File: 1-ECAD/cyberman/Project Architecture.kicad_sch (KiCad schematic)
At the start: 0 parts

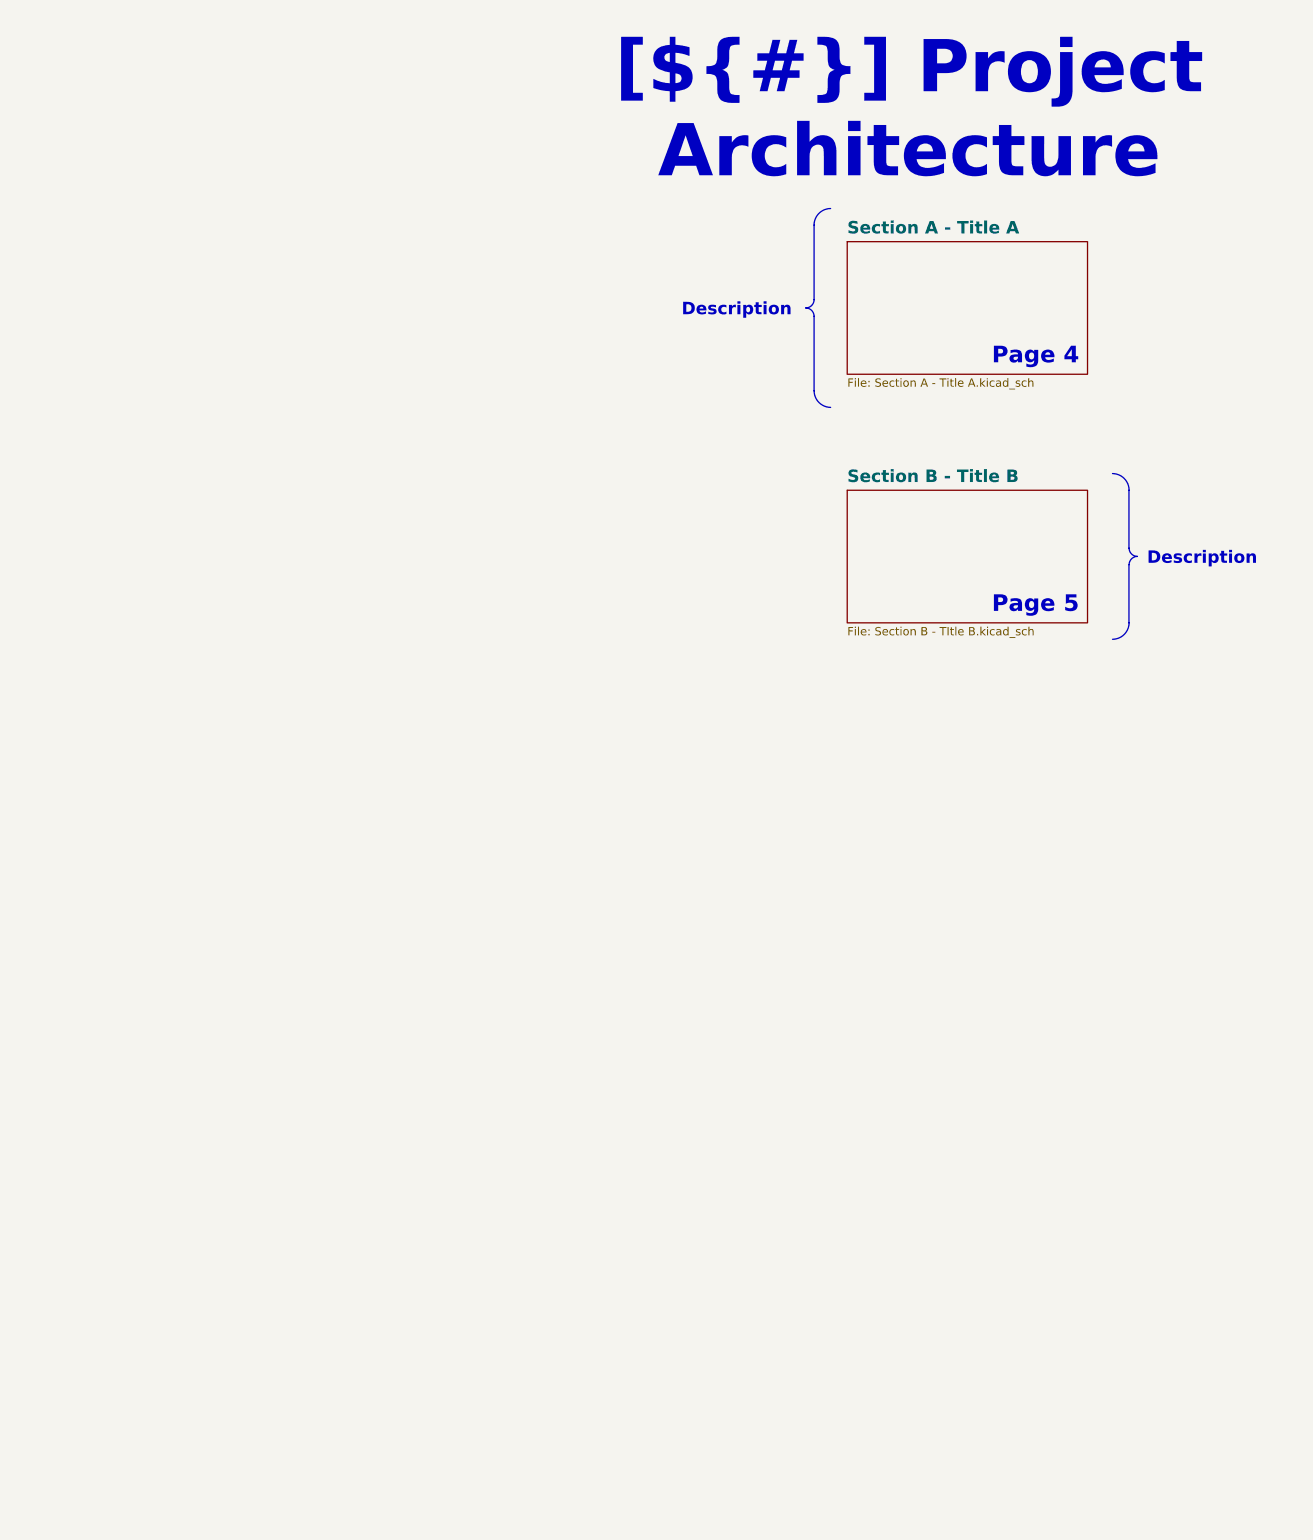
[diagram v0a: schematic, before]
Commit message: esp32 supply
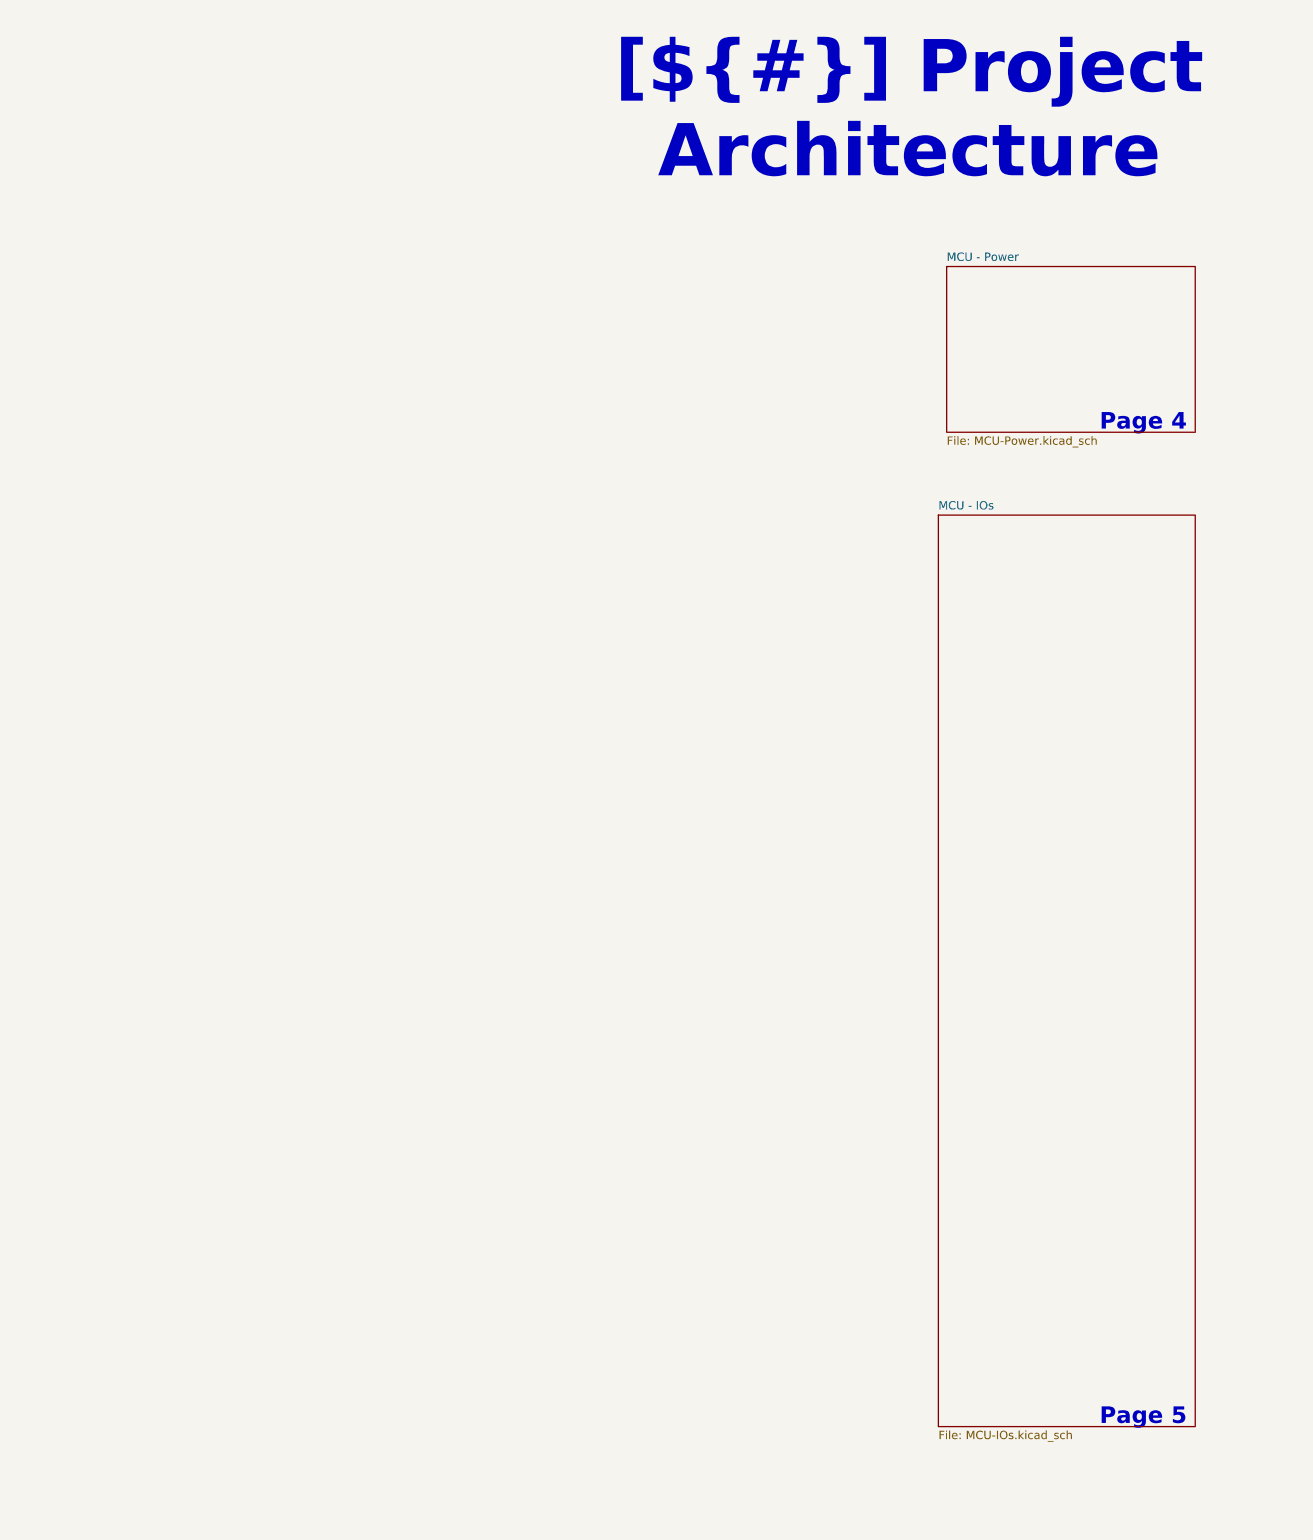
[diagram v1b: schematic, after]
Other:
- removed sheet Section A - Title A
- removed sheet Section B - Title B
- added sheet MCU - IOs (MCU-IOs.kicad_sch)
- added sheet MCU - Power (MCU-Power.kicad_sch)
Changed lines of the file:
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@@
 		(company "${COMPANY}")
-	)
-	(polyline
-		(pts
-			(xy 195.58 58.42) (xy 195.58 69.85)
-		)
-		(stroke
-			(width 0)
-			(type default)
-		)
-	)
-	(polyline
-		(pts
-			(xy 195.58 55.88) (xy 195.58 44.45)
-		)
-		(stroke
-			(width 0)
-			(type default)
-		)
-	)
-	(polyline
-		(pts
-			(xy 243.84 85.09) (xy 243.84 93.98)
-		)
-		(stroke
-			(width 0)
-			(type default)
-		)
-	)
-	(polyline
-		(pts
-			(xy 243.84 96.52) (xy 243.84 105.41)
-		)
-		(stroke
-			(width 0)
-			(type default)
-		)
-	)
-	(arc
-		(start 243.86 96.5)
-		(mid 244.2349 95.6049)
-		(end 245.13 95.23)
-		(stroke
-			(width 0)
-			(type default)
-		)
-		(fill
-			(type none)
-		)
-	)
-	(arc
-		(start 195.58 55.88)
-		(mid 195.2051 56.7751)
-		(end 194.31 57.15)
-		(stroke
-			(width 0)
-			(type default)
-		)
-		(fill
-			(type none)
-		)
-	)
-	(arc
-		(start 241.32 82.53)
-		(mid 243.1102 83.2798)
-		(end 243.86 85.07)
-		(stroke
-			(width 0)
-			(type default)
-		)
-		(fill
-			(type none)
-		)
-	)
-	(arc
-		(start 194.31 57.15)
-		(mid 195.2051 57.5249)
-		(end 195.58 58.42)
-		(stroke
-			(width 0)
-			(type default)
-		)
-		(fill
-			(type none)
-		)
-	)
-	(arc
-		(start 243.86 105.39)
-		(mid 243.1161 107.1861)
-		(end 241.32 107.93)
-		(stroke
-			(width 0)
-			(type default)
-		)
-		(fill
-			(type none)
-		)
-	)
-	(arc
-		(start 245.13 95.23)
-		(mid 244.2349 94.8551)
-		(end 243.86 93.96)
-		(stroke
-			(width 0)
-			(type default)
-		)
-		(fill
-			(type none)
-		)
-	)
-	(arc
-		(start 195.58 44.45)
-		(mid 196.3239 42.6539)
-		(end 198.12 41.91)
-		(stroke
-			(width 0)
-			(type default)
-		)
-		(fill
-			(type none)
-		)
-	)
-	(arc
-		(start 198.12 72.39)
-		(mid 196.3298 71.6402)
-		(end 195.58 69.85)
-		(stroke
-			(width 0)
-			(type default)
-		)
-		(fill
-			(type none)
-		)
-	)
-	(text_box "Description"
-		(exclude_from_sim no)
-		(at 176.53 54.61 0)
-		(size 17.145 5.08)
-		(stroke
-			(width -0.0001)
-			(type default)
-		)
-		(fill
-			(type none)
-		)
-		(effects
-			(font
-				(size 1.905 1.905)
-				(thickness 0.381)
-				(bold yes)
-				(color 0 0 0 1)
-			)
-			(justify right top)
-		)
 	)
 	(text_box "[${#}] ${TITLE}"
@@
 		)
 	)
-	(text_box "Description"
-		(exclude_from_sim no)
-		(at 245.11 92.71 0)
-		(size 26.015 5.1)
-		(stroke
-			(width -0.0001)
-			(type default)
-		)
-		(fill
-			(type none)
-		)
-		(effects
-			(font
-				(size 1.905 1.905)
-				(thickness 0.381)
-				(bold yes)
-				(color 0 0 0 1)
-			)
-			(justify left top)
-		)
-	)
 	(text "Page 4"
 		(exclude_from_sim no)
-		(at 236.22 66.04 0)
+		(at 252.73 76.2 0)
 		(effects
 			(font
@@
 	(text "Page 5"
 		(exclude_from_sim no)
-		(at 236.22 104.14 0)
+		(at 252.73 228.6 0)
 		(effects
 			(font
@@
 	)
 	(sheet
-		(at 200.66 46.99)
-		(size 36.83 20.32)
+		(at 215.9 50.8)
+		(size 38.1 25.4)
 		(fields_autoplaced yes)
 		(stroke
@@
 		)
 		(fill
-			(color 128 255 128 0.5000)
+			(color 0 194 0 0.5000)
 		)
-		(property "Sheetname" "Section A - Title A"
-			(at 200.66 45.9609 0)
+		(property "Sheetname" "MCU - Power"
+			(at 215.9 50.0884 0)
 			(effects
 				(font
-					(size 1.905 1.905)
-					(bold yes)
+					(size 1.27 1.27)
 				)
 				(justify left bottom)
 			)
 		)
-		(property "Sheetfile" "Section A - Title A.kicad_sch"
-			(at 200.66 67.8946 0)
+		(property "Sheetfile" "MCU-Power.kicad_sch"
+			(at 215.9 76.7846 0)
 			(effects
 				(font
-					(face "Arial")
 					(size 1.27 1.27)
 				)
@@
 	)
 	(sheet
-		(at 200.66 85.09)
-		(size 36.83 20.32)
+		(at 214.63 88.9)
+		(size 39.37 139.7)
 		(fields_autoplaced yes)
 		(stroke
@@
 		)
 		(fill
-			(color 255 200 0 0.5020)
+			(color 0 255 255 0.5000)
 		)
-		(property "Sheetname" "Section B - Title B"
-			(at 200.66 84.0609 0)
+		(property "Sheetname" "MCU - IOs"
+			(at 214.63 88.1884 0)
 			(effects
 				(font
-					(size 1.905 1.905)
-					(bold yes)
+					(size 1.27 1.27)
 				)
 				(justify left bottom)
 			)
 		)
-		(property "Sheetfile" "Section B - TItle B.kicad_sch"
-			(at 200.66 105.9946 0)
+		(property "Sheetfile" "MCU-IOs.kicad_sch"
+			(at 214.63 229.1846 0)
 			(effects
 				(font
-					(face "Arial")
 					(size 1.27 1.27)
 				)

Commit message: power
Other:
- added sheet Power (power.kicad_sch)
- sheet MCU - IOs: file MCU-IOs.kicad_sch -> mcu-IOs.kicad_sch
- sheet MCU - Power: file MCU-Power.kicad_sch -> mcu-power.kicad_sch
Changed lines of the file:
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@@
 	(text "Page 4"
 		(exclude_from_sim no)
-		(at 252.73 76.2 0)
+		(at 252.73 74.93 0)
 		(effects
 			(font
@@
 	(text "Page 5"
 		(exclude_from_sim no)
-		(at 252.73 228.6 0)
+		(at 252.73 227.33 0)
 		(effects
 			(font
@@
 			(justify right bottom)
 			(href "#5")
+		)
+	)
+	(sheet
+		(at 88.9 50.8)
+		(size 38.1 25.4)
+		(fields_autoplaced yes)
+		(stroke
+			(width 0.1524)
+			(type solid)
+		)
+		(fill
+			(color 255 0 0 0.5000)
+		)
+		(property "Sheetname" "Power"
+			(at 88.9 50.0884 0)
+			(effects
+				(font
+					(size 1.27 1.27)
+				)
+				(justify left bottom)
+			)
+		)
+		(property "Sheetfile" "power.kicad_sch"
+			(at 88.9 76.7846 0)
+			(effects
+				(font
+					(size 1.27 1.27)
+				)
+				(justify left top)
+			)
+		)
+		(instances
+			(project "cyberman"
+				(path "/0650c7a8-acba-429c-9f8e-eec0baf0bc1c/fede4c36-00cc-4d3d-b71c-5243ba232202"
+					(page "7")
+				)
+			)
 		)
 	)
@@
 			)
 		)
-		(property "Sheetfile" "MCU-Power.kicad_sch"
+		(property "Sheetfile" "mcu-power.kicad_sch"
 			(at 215.9 76.7846 0)
 			(effects
@@
 			)
 		)
-		(property "Sheetfile" "MCU-IOs.kicad_sch"
+		(property "Sheetfile" "mcu-IOs.kicad_sch"
 			(at 214.63 229.1846 0)
 			(effects

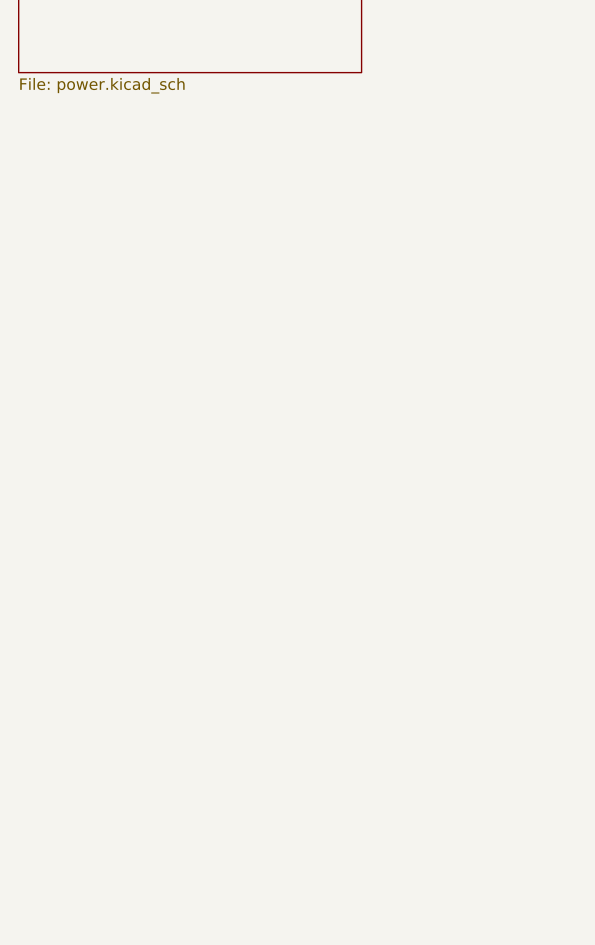
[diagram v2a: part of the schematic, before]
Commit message: microSD and LCD connector
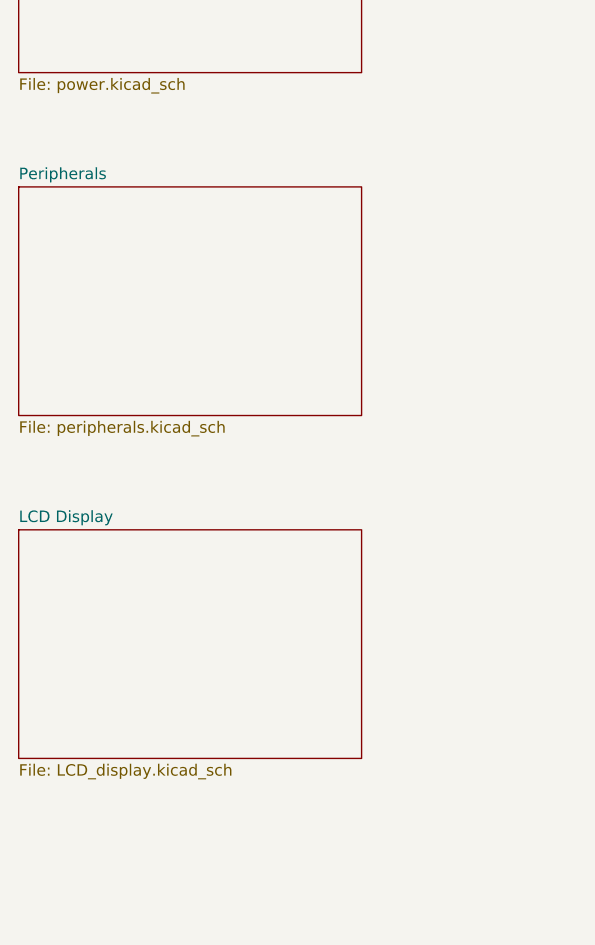
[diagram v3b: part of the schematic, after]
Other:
- added sheet LCD Display (LCD_display.kicad_sch)
- added sheet Peripherals (peripherals.kicad_sch)
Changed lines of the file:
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@@
+	)
+	(sheet
+		(at 88.9 127)
+		(size 38.1 25.4)
+		(fields_autoplaced yes)
+		(stroke
+			(width 0.1524)
+			(type solid)
+		)
+		(fill
+			(color 0 255 0 0.5000)
+		)
+		(property "Sheetname" "LCD Display"
+			(at 88.9 126.2884 0)
+			(effects
+				(font
+					(size 1.27 1.27)
+				)
+				(justify left bottom)
+			)
+		)
+		(property "Sheetfile" "LCD_display.kicad_sch"
+			(at 88.9 152.9846 0)
+			(effects
+				(font
+					(size 1.27 1.27)
+				)
+				(justify left top)
+			)
+		)
+		(instances
+			(project "cyberman"
+				(path "/0650c7a8-acba-429c-9f8e-eec0baf0bc1c/fede4c36-00cc-4d3d-b71c-5243ba232202"
+					(page "9")
+				)
+			)
+		)
+	)
+	(sheet
+		(at 88.9 88.9)
+		(size 38.1 25.4)
+		(fields_autoplaced yes)
+		(stroke
+			(width 0.1524)
+			(type solid)
+		)
+		(fill
+			(color 255 153 0 0.5000)
+		)
+		(property "Sheetname" "Peripherals"
+			(at 88.9 88.1884 0)
+			(effects
+				(font
+					(size 1.27 1.27)
+				)
+				(justify left bottom)
+			)
+		)
+		(property "Sheetfile" "peripherals.kicad_sch"
+			(at 88.9 114.8846 0)
+			(effects
+				(font
+					(size 1.27 1.27)
+				)
+				(justify left top)
+			)
+		)
+		(instances
+			(project "cyberman"
+				(path "/0650c7a8-acba-429c-9f8e-eec0baf0bc1c/fede4c36-00cc-4d3d-b71c-5243ba232202"
+					(page "8")
+				)
+			)
+		)
 	)
 	(sheet

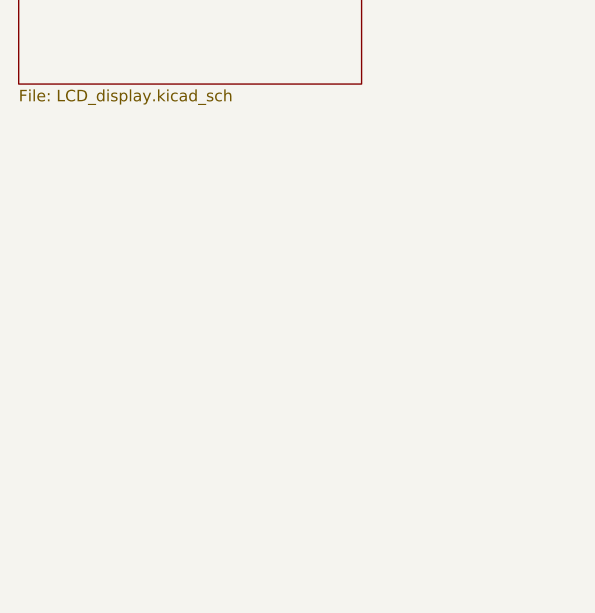
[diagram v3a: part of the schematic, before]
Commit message: add sensor page
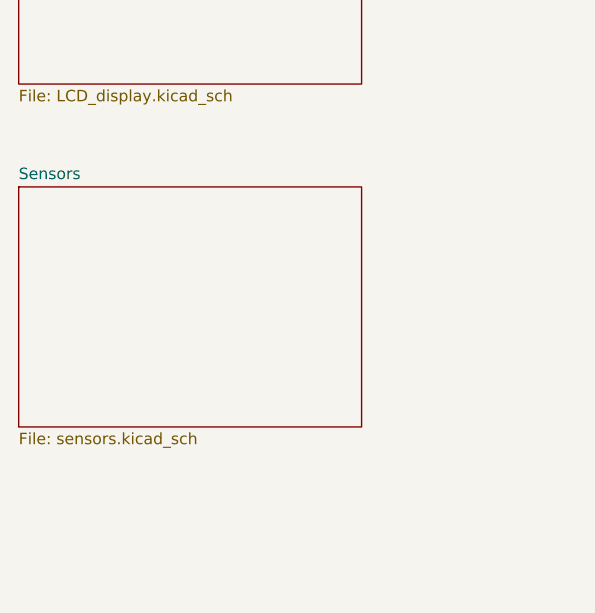
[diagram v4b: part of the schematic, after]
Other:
- added sheet Sensors (sensors.kicad_sch)
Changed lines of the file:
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@@
+	)
+	(sheet
+		(at 88.9 163.83)
+		(size 38.1 26.67)
+		(fields_autoplaced yes)
+		(stroke
+			(width 0.1524)
+			(type solid)
+		)
+		(fill
+			(color 255 0 255 0.5000)
+		)
+		(property "Sheetname" "Sensors"
+			(at 88.9 163.1184 0)
+			(effects
+				(font
+					(size 1.27 1.27)
+				)
+				(justify left bottom)
+			)
+		)
+		(property "Sheetfile" "sensors.kicad_sch"
+			(at 88.9 191.0846 0)
+			(effects
+				(font
+					(size 1.27 1.27)
+				)
+				(justify left top)
+			)
+		)
+		(instances
+			(project "cyberman"
+				(path "/0650c7a8-acba-429c-9f8e-eec0baf0bc1c/fede4c36-00cc-4d3d-b71c-5243ba232202"
+					(page "10")
+				)
+			)
+		)
 	)
 	(sheet
